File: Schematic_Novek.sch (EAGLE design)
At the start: 22 parts, among them IC1 STM32F10XCXT6, U1 BQ21040

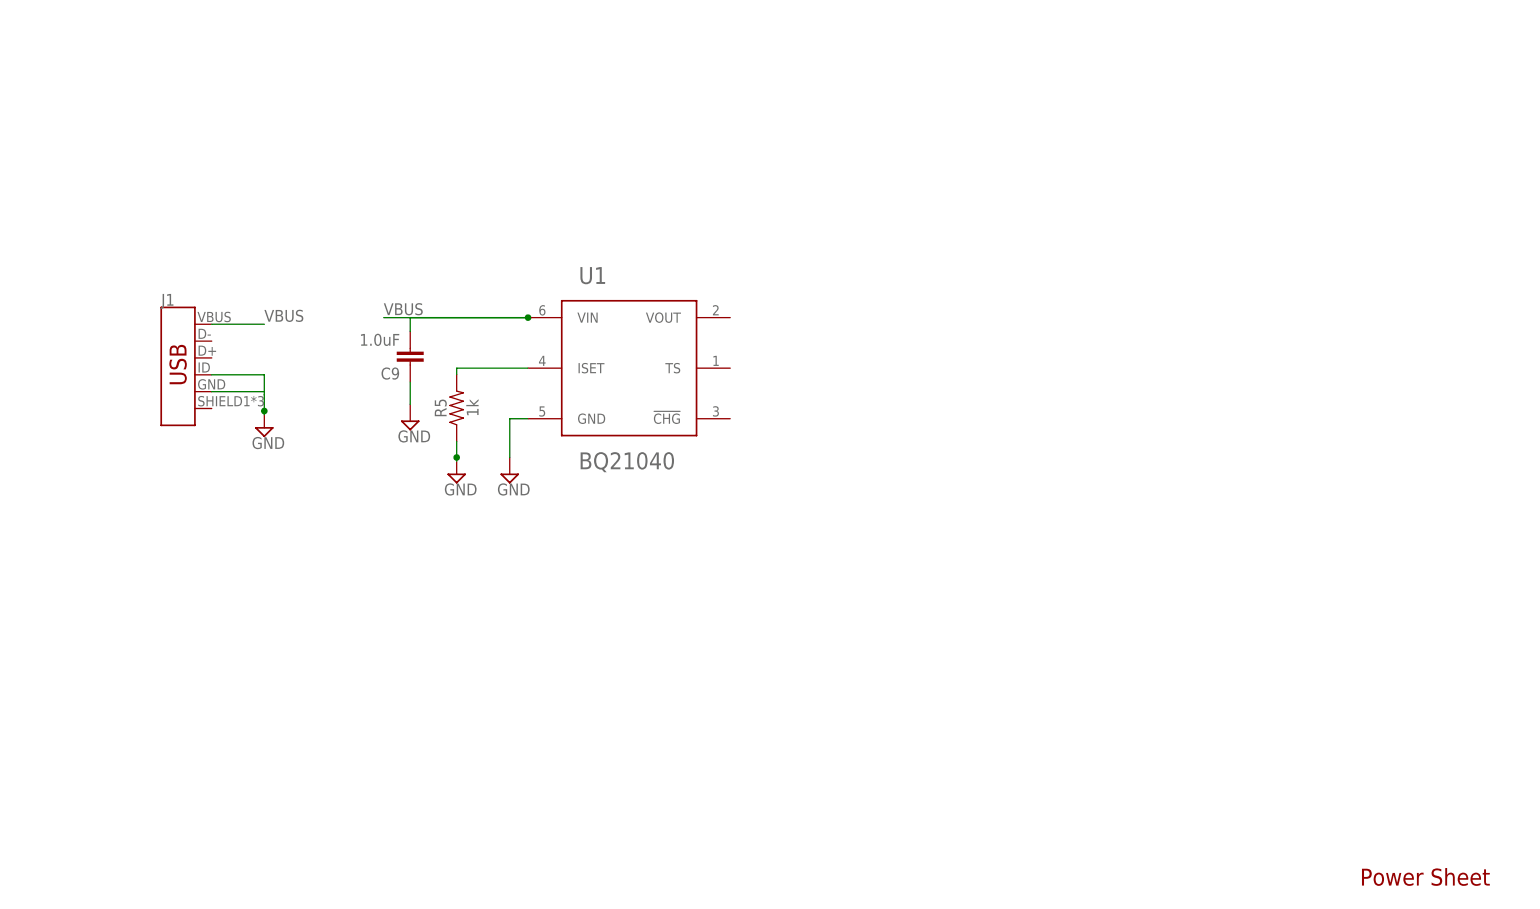
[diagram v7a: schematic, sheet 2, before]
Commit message: adds 3.3V LDO
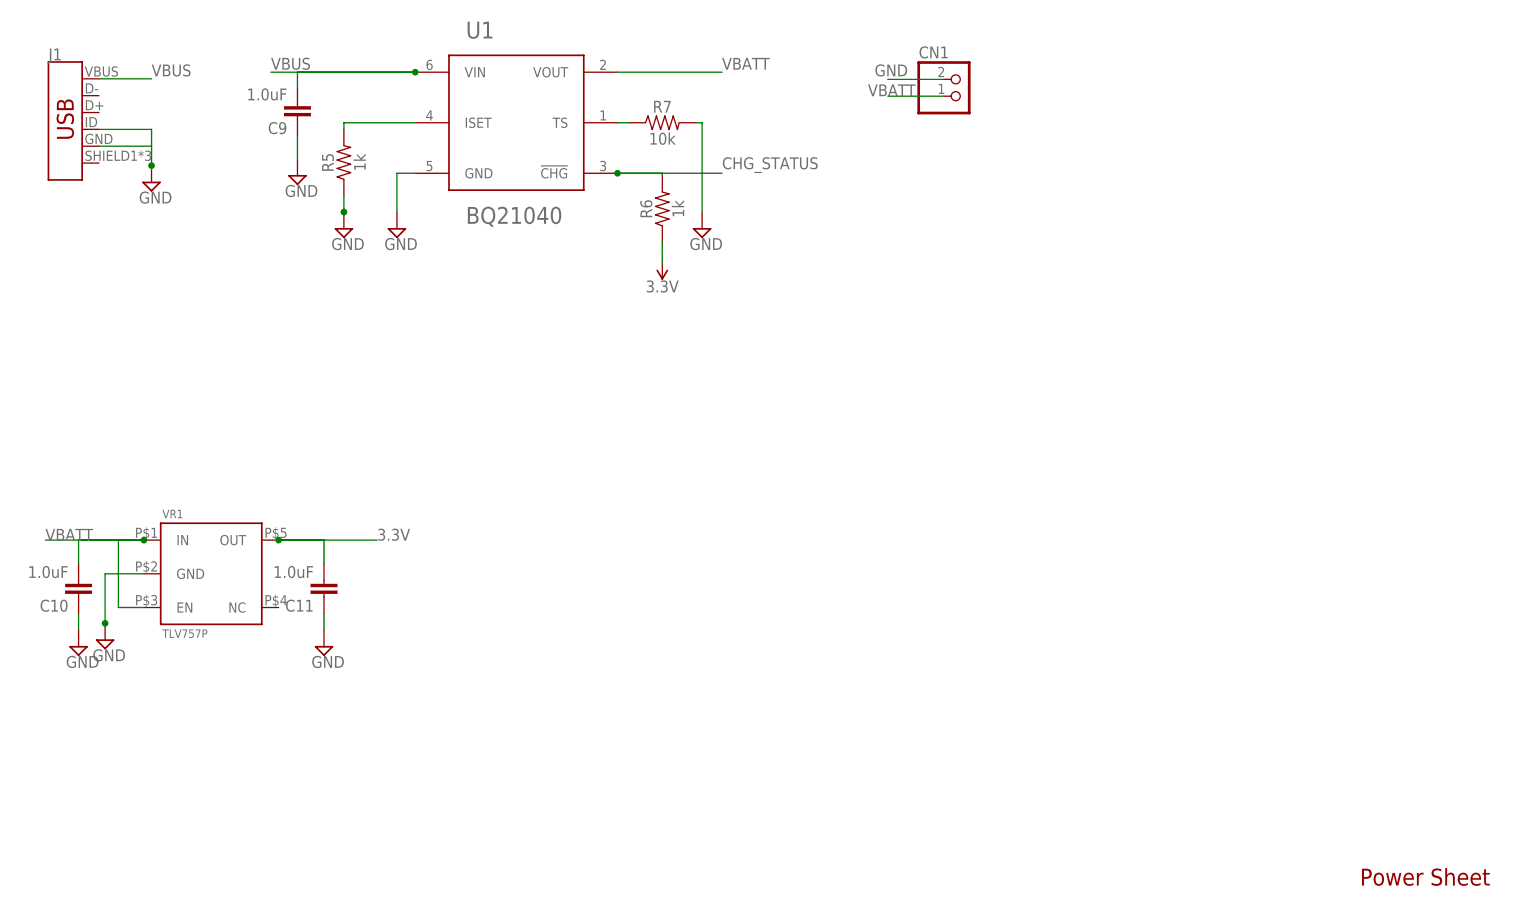
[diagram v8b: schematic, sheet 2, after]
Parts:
- added C10, C11: 1.0uF, SparkFun-Capacitors:1.0UF-0603-16V-10%
- added CN1: (no value), adafruit:JST_2PIN-THM
- added R6: 1k, SparkFun-Resistors:1KOHM-0603-1/10W-1%
- added R7: 10k, SparkFun-Resistors:10KOHM-0603-1/10W-1%
- added VR1: TLV757P, TLV757P:TLV757P
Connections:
- new net CHG_STATUS: R6.2, U1.!CHG!
- new net N$2: R7.1, U1.TS
- new net VBATT: C10.2, CN1.2, U1.VOUT, VR1.EN, VR1.IN
- net 3.3V: now also C11.2, R6.1, VR1.OUT
- net GND: now also C10.1, C11.1, CN1.1, R7.2, VR1.GND
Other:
- moved on the sheet: C9, J1, R5, U1
